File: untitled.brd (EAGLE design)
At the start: 100 x 80 mm, 7 parts

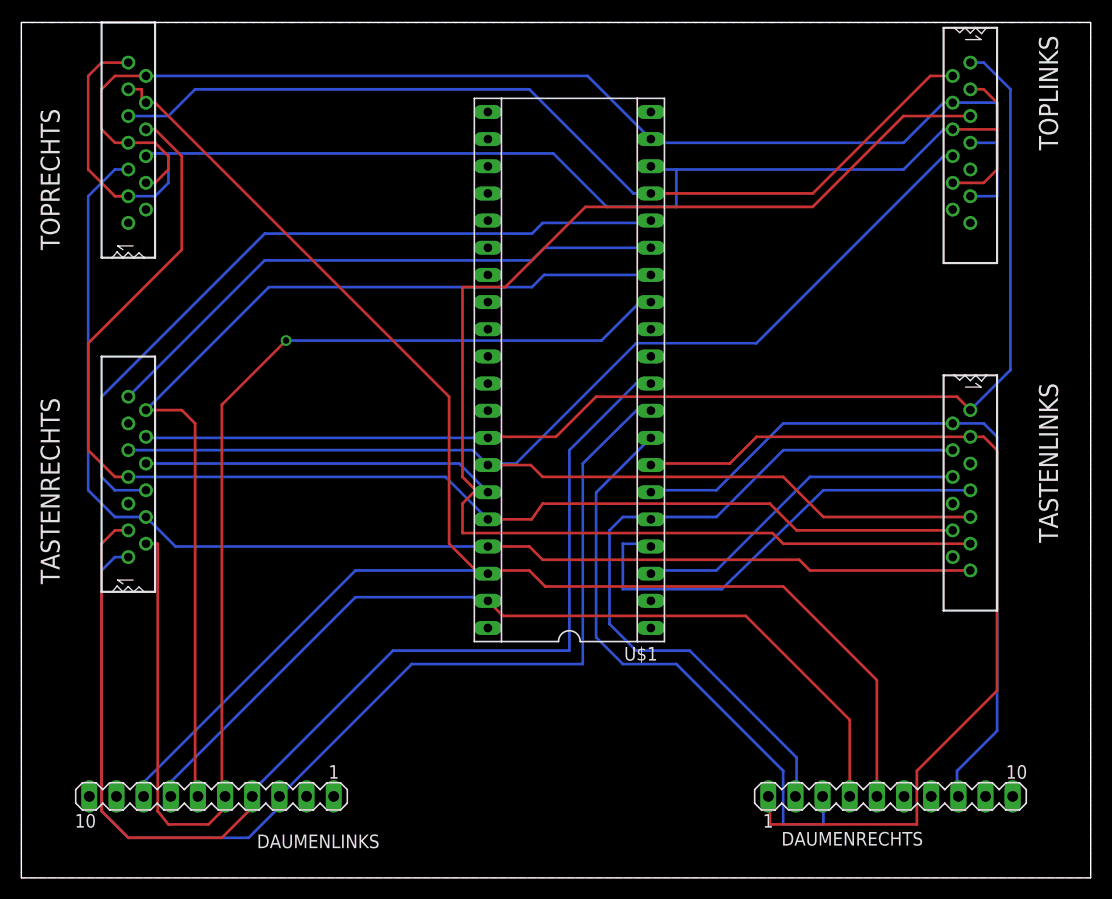
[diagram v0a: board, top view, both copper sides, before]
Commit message: circuit path alignment
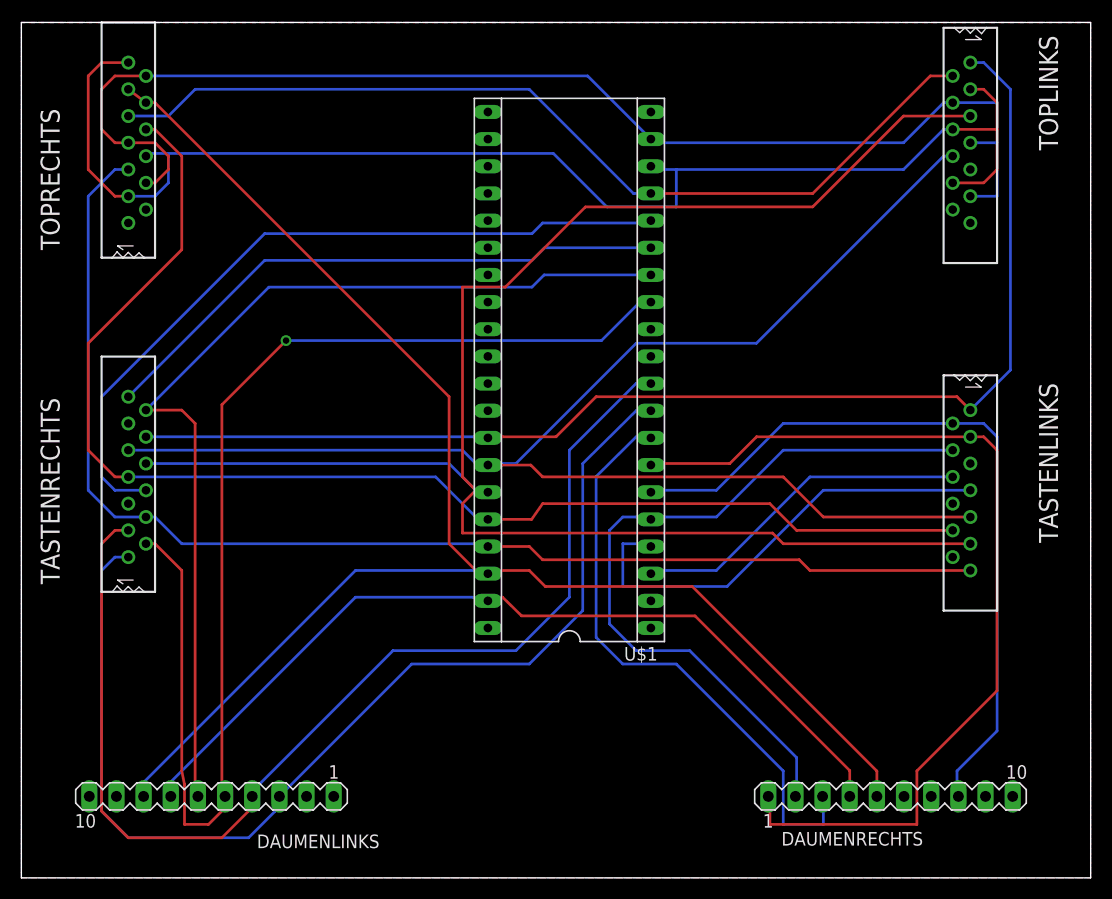
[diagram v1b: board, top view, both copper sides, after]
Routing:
- net B5: track 154.7 -> 148.9 mm
- net D7: track 109.9 -> 107.0 mm
- net D6: track 106.2 -> 103.2 mm
- net B6: track 83.9 -> 81.3 mm
- net C0: track 115.4 -> 114.3 mm
- net D5: track 54.8 -> 55.8 mm
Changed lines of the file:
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@@
 <wire x1="57.75" y1="53.75" x2="58.87" y2="53.85" width="0.254" layer="16"/>
 <via x="24.75" y="50.25" extent="1-16" drill="0.6096"/>
-<wire x1="11.65" y1="31.25" x2="12.75" y2="31.25" width="0.254" layer="1"/>
-<wire x1="12.75" y1="31.25" x2="12.75" y2="6.25" width="0.254" layer="1"/>
-<wire x1="12.75" y1="6.25" x2="13.75" y2="5" width="0.254" layer="1"/>
-<wire x1="13.75" y1="5" x2="17.5" y2="5" width="0.254" layer="1"/>
+<wire x1="11.65" y1="31.25" x2="12.5" y2="31.25" width="0.254" layer="1"/>
+<wire x1="12.5" y1="31.25" x2="15" y2="28.75" width="0.254" layer="1"/>
+<wire x1="15" y1="28.75" x2="15" y2="10" width="0.254" layer="1"/>
+<wire x1="15" y1="10" x2="15.25" y2="8.75" width="0.254" layer="1"/>
+<wire x1="15.25" y1="8.75" x2="15.25" y2="5" width="0.254" layer="1"/>
+<wire x1="15.25" y1="5" x2="17.5" y2="5" width="0.254" layer="1"/>
 <wire x1="17.5" y1="5" x2="18.75" y2="6.25" width="0.254" layer="1"/>
 <wire x1="18.75" y1="6.25" x2="19.05" y2="7.62" width="0.254" layer="1"/>
@@
 <wire x1="61.25" y1="20" x2="56.25" y2="20" width="0.254" layer="16"/>
 <wire x1="56.25" y1="20" x2="53.75" y2="22.5" width="0.254" layer="16"/>
-<wire x1="53.75" y1="22.5" x2="53.75" y2="36.03" width="0.254" layer="16"/>
-<wire x1="53.75" y1="36.03" x2="58.87" y2="41.15" width="0.254" layer="16"/>
+<wire x1="53.75" y1="22.5" x2="53.75" y2="37.53" width="0.254" layer="16"/>
+<wire x1="53.75" y1="37.53" x2="57.5" y2="41.25" width="0.254" layer="16"/>
+<wire x1="57.5" y1="41.25" x2="58.87" y2="41.15" width="0.254" layer="16"/>
 </signal>
 <signal name="D6">
@@
 <wire x1="58.87" y1="43.69" x2="57.56" y2="43.75" width="0.254" layer="16"/>
 <wire x1="57.56" y1="43.75" x2="52.5" y2="38.75" width="0.254" layer="16"/>
-<wire x1="52.5" y1="38.75" x2="52.5" y2="20" width="0.254" layer="16"/>
-<wire x1="52.5" y1="20" x2="36.51" y2="20" width="0.254" layer="16"/>
+<wire x1="52.5" y1="38.75" x2="52.5" y2="25" width="0.254" layer="16"/>
+<wire x1="52.5" y1="25" x2="47.5" y2="20" width="0.254" layer="16"/>
+<wire x1="47.5" y1="20" x2="36.51" y2="20" width="0.254" layer="16"/>
 <wire x1="36.51" y1="20" x2="24.13" y2="7.62" width="0.254" layer="16"/>
 </signal>
@@
 <wire x1="21.75" y1="8.25" x2="21.59" y2="7.62" width="0.254" layer="16"/>
 <wire x1="57.5" y1="46.25" x2="51.25" y2="40" width="0.254" layer="16"/>
-<wire x1="51.25" y1="40" x2="51.25" y2="21.25" width="0.254" layer="16"/>
-<wire x1="51.25" y1="21.25" x2="34.75" y2="21.25" width="0.254" layer="16"/>
+<wire x1="51.25" y1="40" x2="51.25" y2="26.25" width="0.254" layer="16"/>
+<wire x1="51.25" y1="26.25" x2="46.25" y2="21.25" width="0.254" layer="16"/>
+<wire x1="46.25" y1="21.25" x2="34.75" y2="21.25" width="0.254" layer="16"/>
 <wire x1="34.75" y1="21.25" x2="21.75" y2="8.25" width="0.254" layer="16"/>
 </signal>
@@
 <wire x1="92.5" y1="73.75" x2="90" y2="76.25" width="0.254" layer="16"/>
 <wire x1="90" y1="76.25" x2="88.75" y2="76.25" width="0.254" layer="16"/>
-<wire x1="43.63" y1="41.15" x2="11.75" y2="41.15" width="0.254" layer="16"/>
-<wire x1="11.75" y1="41.15" x2="11.65" y2="41.25" width="0.254" layer="16"/>
+<wire x1="43.63" y1="41.15" x2="42.5" y2="41.25" width="0.254" layer="16"/>
+<wire x1="42.5" y1="41.25" x2="11.75" y2="41.25" width="0.254" layer="16"/>
+<wire x1="11.75" y1="41.25" x2="11.65" y2="41.25" width="0.254" layer="16"/>
 <wire x1="43.63" y1="41.15" x2="45" y2="41.25" width="0.254" layer="1"/>
 <wire x1="45" y1="41.25" x2="50" y2="41.25" width="0.254" layer="1"/>
@@
 <wire x1="48.75" y1="37.5" x2="47.64" y2="38.61" width="0.254" layer="1"/>
 <wire x1="47.64" y1="38.61" x2="43.63" y2="38.61" width="0.254" layer="1"/>
-<wire x1="10" y1="40" x2="42.24" y2="40" width="0.254" layer="16"/>
-<wire x1="42.24" y1="40" x2="43.63" y2="38.61" width="0.254" layer="16"/>
+<wire x1="10" y1="40" x2="41.25" y2="40" width="0.254" layer="16"/>
+<wire x1="41.25" y1="40" x2="42.5" y2="38.75" width="0.254" layer="16"/>
+<wire x1="42.5" y1="38.75" x2="43.63" y2="38.61" width="0.254" layer="16"/>
 <wire x1="87.1" y1="67.5" x2="86.25" y2="67.5" width="0.254" layer="16"/>
 <wire x1="86.25" y1="67.5" x2="68.75" y2="50" width="0.254" layer="16"/>
@@
 <wire x1="42.5" y1="36.25" x2="43.45" y2="36.25" width="0.254" layer="1"/>
 <wire x1="43.45" y1="36.25" x2="43.63" y2="36.07" width="0.254" layer="1"/>
-<wire x1="11.65" y1="38.75" x2="40.95" y2="38.75" width="0.254" layer="16"/>
-<wire x1="40.95" y1="38.75" x2="43.63" y2="36.07" width="0.254" layer="16"/>
+<wire x1="11.65" y1="38.75" x2="40" y2="38.75" width="0.254" layer="16"/>
+<wire x1="40" y1="38.75" x2="42.5" y2="36.25" width="0.254" layer="16"/>
+<wire x1="42.5" y1="36.25" x2="43.63" y2="36.07" width="0.254" layer="16"/>
 <wire x1="88.75" y1="71.25" x2="82.5" y2="71.25" width="0.254" layer="1"/>
 <wire x1="82.5" y1="71.25" x2="74" y2="62.75" width="0.254" layer="1"/>
@@
 <wire x1="6.25" y1="36.25" x2="8.75" y2="33.75" width="0.254" layer="16"/>
 <wire x1="8.75" y1="33.75" x2="11.65" y2="33.75" width="0.254" layer="16"/>
-<wire x1="11.65" y1="33.75" x2="14.41" y2="30.99" width="0.254" layer="16"/>
-<wire x1="14.41" y1="30.99" x2="43.63" y2="30.99" width="0.254" layer="16"/>
+<wire x1="11.65" y1="33.75" x2="12.5" y2="33.75" width="0.254" layer="16"/>
+<wire x1="12.5" y1="33.75" x2="15" y2="31.25" width="0.254" layer="16"/>
+<wire x1="15" y1="31.25" x2="42.5" y2="31.25" width="0.254" layer="16"/>
+<wire x1="42.5" y1="31.25" x2="43.63" y2="30.99" width="0.254" layer="16"/>
 </signal>
 <signal name="B5">
@@
 <contactref element="TOPRECHTS" pad="P$10"/>
 <contactref element="TOPRECHTS" pad="P$11"/>
-<wire x1="80.01" y1="7.62" x2="80.01" y2="18.49" width="0.254" layer="1"/>
-<wire x1="80.01" y1="18.49" x2="71.25" y2="27.25" width="0.254" layer="1"/>
-<wire x1="71.25" y1="27.25" x2="49" y2="27.25" width="0.254" layer="1"/>
+<wire x1="80.01" y1="7.62" x2="80.01" y2="9.99" width="0.254" layer="1"/>
+<wire x1="80.01" y1="9.99" x2="62.75" y2="27.25" width="0.254" layer="1"/>
+<wire x1="62.75" y1="27.25" x2="49" y2="27.25" width="0.254" layer="1"/>
 <wire x1="49" y1="27.25" x2="47.5" y2="28.75" width="0.254" layer="1"/>
 <wire x1="47.5" y1="28.75" x2="43.93" y2="28.75" width="0.254" layer="1"/>
 <wire x1="43.93" y1="28.75" x2="43.63" y2="28.45" width="0.254" layer="1"/>
-<wire x1="11.25" y1="73.75" x2="11.25" y2="72.5" width="0.254" layer="1"/>
-<wire x1="11.25" y1="72.5" x2="11.65" y2="72.5" width="0.254" layer="1"/>
-<wire x1="11.25" y1="73.75" x2="10" y2="73.75" width="0.254" layer="1"/>
 <wire x1="31.25" y1="28.75" x2="11.25" y2="8.75" width="0.254" layer="16"/>
 <wire x1="43.5" y1="28.5" x2="42.75" y2="28.5" width="0.254" layer="16"/>
@@
 <wire x1="12.5" y1="72.5" x2="11.65" y2="72.5" width="0.254" layer="1"/>
 <wire x1="43.5" y1="28.5" x2="43.63" y2="28.45" width="0.254" layer="1"/>
+<wire x1="11.65" y1="72.5" x2="10" y2="73.75" width="0.254" layer="1"/>
 </signal>
 <signal name="B6">
@@
 <contactref element="DAUMENRECHTS" pad="4"/>
 <contactref element="DAUMENLINKS" pad="7"/>
-<wire x1="77.47" y1="7.62" x2="77.47" y2="14.78" width="0.254" layer="1"/>
-<wire x1="77.47" y1="14.78" x2="67.75" y2="24.5" width="0.254" layer="1"/>
-<wire x1="67.75" y1="24.5" x2="45.04" y2="24.5" width="0.254" layer="1"/>
-<wire x1="45.04" y1="24.5" x2="43.63" y2="25.91" width="0.254" layer="1"/>
+<wire x1="77.47" y1="7.62" x2="77.47" y2="10.03" width="0.254" layer="1"/>
+<wire x1="77.47" y1="10.03" x2="63" y2="24.5" width="0.254" layer="1"/>
+<wire x1="63" y1="24.5" x2="46.79" y2="24.5" width="0.254" layer="1"/>
+<wire x1="46.79" y1="24.5" x2="45" y2="26.25" width="0.254" layer="1"/>
+<wire x1="45" y1="26.25" x2="43.63" y2="25.91" width="0.254" layer="1"/>
 <wire x1="31.25" y1="26.25" x2="13.75" y2="8.75" width="0.254" layer="16"/>
 <wire x1="42.25" y1="26.25" x2="31.25" y2="26.25" width="0.254" layer="16"/>
@@
 <wire x1="6.25" y1="40" x2="8.75" y2="37.5" width="0.254" layer="1"/>
 <wire x1="8.75" y1="37.5" x2="10" y2="37.5" width="0.254" layer="1"/>
-<wire x1="10" y1="37.5" x2="39.66" y2="37.5" width="0.254" layer="16"/>
-<wire x1="39.66" y1="37.5" x2="43.63" y2="33.53" width="0.254" layer="16"/>
+<wire x1="10" y1="37.5" x2="38.75" y2="37.5" width="0.254" layer="16"/>
+<wire x1="38.75" y1="37.5" x2="42.5" y2="33.75" width="0.254" layer="16"/>
+<wire x1="42.5" y1="33.75" x2="43.63" y2="33.53" width="0.254" layer="16"/>
 </signal>
 <signal name="D1">
@@
 <contactref element="U$1" pad="D1"/>
 <wire x1="88.75" y1="36.25" x2="75" y2="36.25" width="0.254" layer="16"/>
-<wire x1="75" y1="36.25" x2="65.5" y2="27" width="0.254" layer="16"/>
-<wire x1="65.5" y1="27" x2="56.25" y2="27" width="0.254" layer="16"/>
-<wire x1="56.25" y1="27" x2="56.25" y2="31.25" width="0.254" layer="16"/>
+<wire x1="75" y1="36.25" x2="66" y2="27.25" width="0.254" layer="16"/>
+<wire x1="66" y1="27.25" x2="56.25" y2="27.25" width="0.254" layer="16"/>
+<wire x1="56.25" y1="27.25" x2="56.25" y2="31.25" width="0.254" layer="16"/>
 <wire x1="56.25" y1="31.25" x2="57.88" y2="31.25" width="0.254" layer="16"/>
 <wire x1="57.88" y1="31.25" x2="58.87" y2="30.99" width="0.254" layer="16"/>
